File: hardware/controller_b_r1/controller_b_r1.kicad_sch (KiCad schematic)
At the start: 53 parts, among them J101 Front Pannel Connector, J102 SWD Header, J103 USB Micro B, Q101 NMOS, SW101 Reset Button, SW102 User Button, U101 NCP115ASN330T2G, U102 74LVC2T45HK3, U103 RP2040, U104 W25Q16JVUXIQ, Y101 12MHz

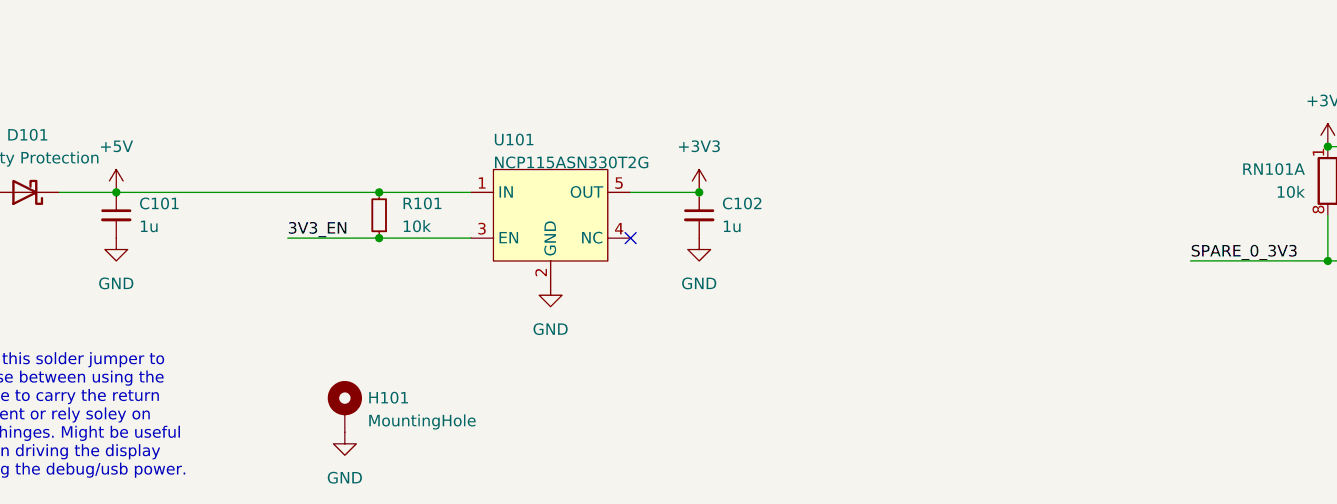
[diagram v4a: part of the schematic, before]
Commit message: First pass at the rev 2 power board.
Only did copper layers on the power board so far. Waiting to decide on a PCB fab house then I'll go back and make sure it's compliant (looking mostly at how close I can pack vias). Starting on the nucleo programmer shield next. Added a voltage divider to the enable pin on the 3V3 vreg on the controller board so it only switches on when there is enough input voltage for correct 3V3 output. I did this because I read somewhere that the RP2040 can power on at a lower voltage than a lot of flash chips and if that happens it gets into a weird state so I'm trying to make sure 3V3 comes on as quickly and sharply as possible.
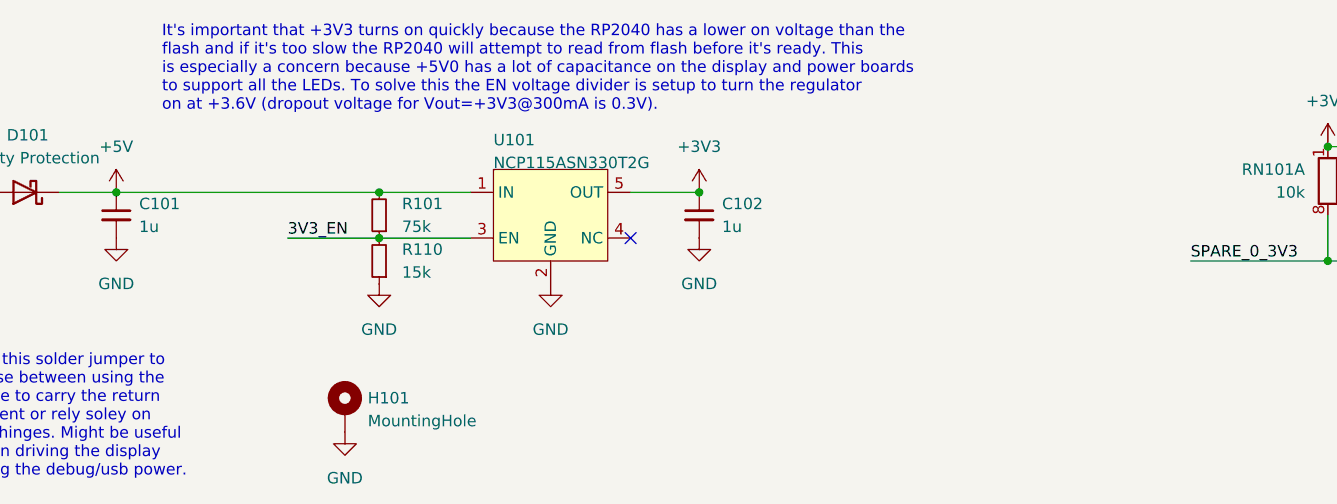
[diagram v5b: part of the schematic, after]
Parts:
- added R110: 15k, Resistor_SMD:R_0402_1005Metric, symbol Device:R_Small
- R101: value 10k -> 75k
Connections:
- net 3V3_EN: now also R110.2
- net GND: now also R110.1
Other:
- note added: "It's important that +3V3 turns on quickly because the RP2040 has a lower on voltage than the flash and if it's too slow the RP2040 will attempt to read from flash before it's ready. This is especially a concern because +5V0 has a lot of capacitance on the display and power boards to support all the LEDs. To solve this the EN voltage divider is setup to turn the regulator on at +3.6V (dropout volt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"
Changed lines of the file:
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@@
     (stroke (width 0) (type default) (color 0 0 0 0))
+  )
+  (text "It's important that +3V3 turns on quickly because the RP2040 has a lower on voltage than the\nflash and if it's too slow the RP2040 will attempt to read from flash before it's ready. This\nis especially a concern because +5V0 has a lot of capacitance on the display and power boards\nto support all the LEDs. To solve this the EN voltage divider is setup to turn the regulator\non at +3.6V (dropout voltage for Vout=+3V3@300mA is 0.3V).\n"
+    (at 77.47 25.4 0)
+    (effects (font (size 1.27 1.27)) (justify left bottom))
   )
   (text "PWM_3_A" (at 283.21 172.72 0)
@@
       (effects (font (size 1.27 1.27)) (justify right))
     )
-    (property "Value" "10k" (id 1) (at 104.14 38.0999 0)
+    (property "Value" "75k" (id 1) (at 104.14 38.0999 0)
       (effects (font (size 1.27 1.27)) (justify right))
     )
@@
     (pin "1")
   )
+  (symbol (lib_id "power:GND") (at 101.6 44.45 0) (unit 1)
+    (in_bom yes) (on_board yes) (fields_autoplaced)
+    (property "Reference" "#PWR0151" (id 0) (at 101.6 50.8 0)
+      (effects (font (size 1.27 1.27)) hide)
+    )
+    (property "Value" "GND" (id 1) (at 101.6 49.53 0))
+    (property "Footprint" "" (id 2) (at 101.6 44.45 0)
+      (effects (font (size 1.27 1.27)) hide)
+    )
+    (property "Datasheet" "" (id 3) (at 101.6 44.45 0)
+      (effects (font (size 1.27 1.27)) hide)
+    )
+    (pin "1")
+  )
   (symbol (lib_id "power:GND") (at 137.16 39.37 0) (unit 1)
     (in_bom yes) (on_board yes) (fields_autoplaced)
@@
     (pin "5")
   )
+  (symbol (lib_id "Device:R_Small") (at 101.6 41.91 180) (unit 1)
+    (in_bom yes) (on_board yes) (fields_autoplaced)
+    (property "Reference" "R110" (id 0) (at 104.14 40.6399 0)
+      (effects (font (size 1.27 1.27)) (justify right))
+    )
+    (property "Value" "15k" (id 1) (at 104.14 43.1799 0)
+      (effects (font (size 1.27 1.27)) (justify right))
+    )
+    (property "Footprint" "Resistor_SMD:R_0402_1005Metric" (id 2) (at 101.6 41.91 0)
+      (effects (font (size 1.27 1.27)) hide)
+    )
+    (property "Datasheet" "~" (id 3) (at 101.6 41.91 0)
+      (effects (font (size 1.27 1.27)) hide)
+    )
+    (pin "1")
+    (pin "2")
+  )
   (symbol (lib_id "Jumper:SolderJumper_2_Open") (at 330.2 217.17 90) (unit 1)
     (in_bom yes) (on_board yes)
@@
       (reference "#PWR0150") (unit 1) (value "VDD") (footprint "")
     )
+    (path "/9e79f1f1-5f45-41a0-96ff-06d6b5bd2da7"
+      (reference "#PWR0151") (unit 1) (value "GND") (footprint "")
+    )
     (path "/db515d74-3d0b-477b-8e05-e548a429c513"
       (reference "C101") (unit 1) (value "1u") (footprint "Capacitor_SMD:C_0402_1005Metric")
@@
     )
     (path "/82bcf8a8-0208-404b-8bd2-25710fbe3f5d"
-      (reference "R101") (unit 1) (value "10k") (footprint "Resistor_SMD:R_0402_1005Metric")
+      (reference "R101") (unit 1) (value "75k") (footprint "Resistor_SMD:R_0402_1005Metric")
     )
     (path "/901630b6-acce-49bc-9a7c-e09bfc7be616"
@@
       (reference "R109") (unit 1) (value "1k") (footprint "Resistor_SMD:R_0402_1005Metric")
     )
+    (path "/b9607c09-e293-4332-83e9-c1e94077ce90"
+      (reference "R110") (unit 1) (value "15k") (footprint "Resistor_SMD:R_0402_1005Metric")
+    )
     (path "/b68868d2-8513-482d-974f-9ce023751b7f"

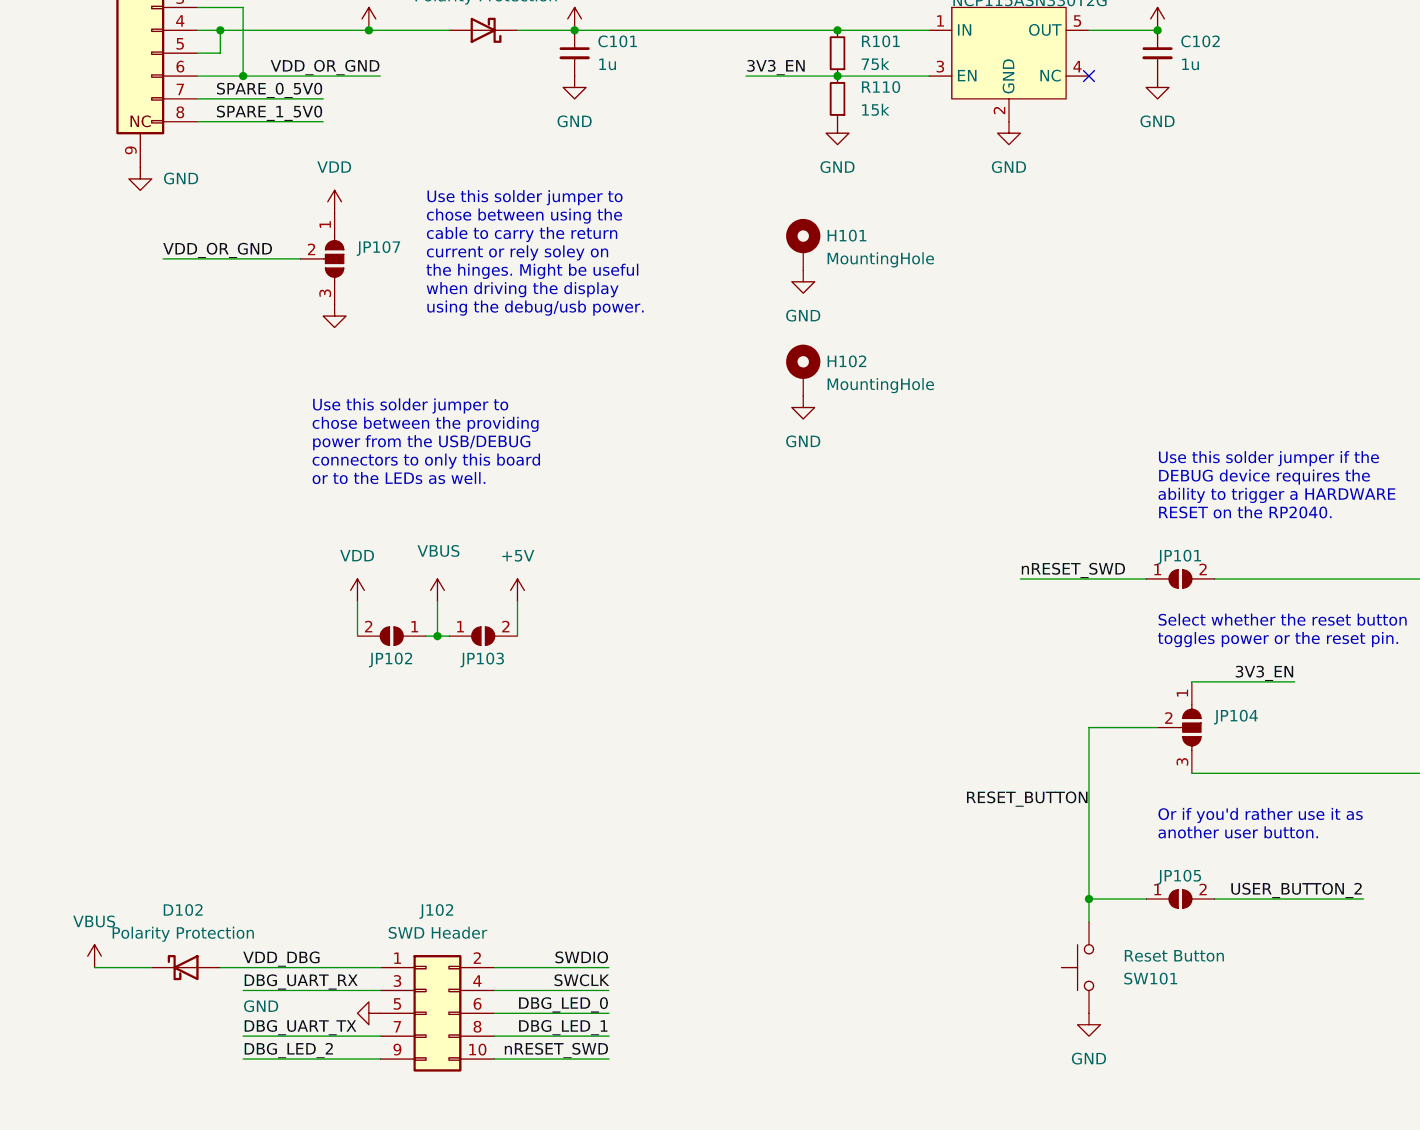
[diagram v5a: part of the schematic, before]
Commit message: Next revision of the boards are finished and ready for fabrication, and a BOM has been added.
The BOM is still missing components for the nucleo shield.
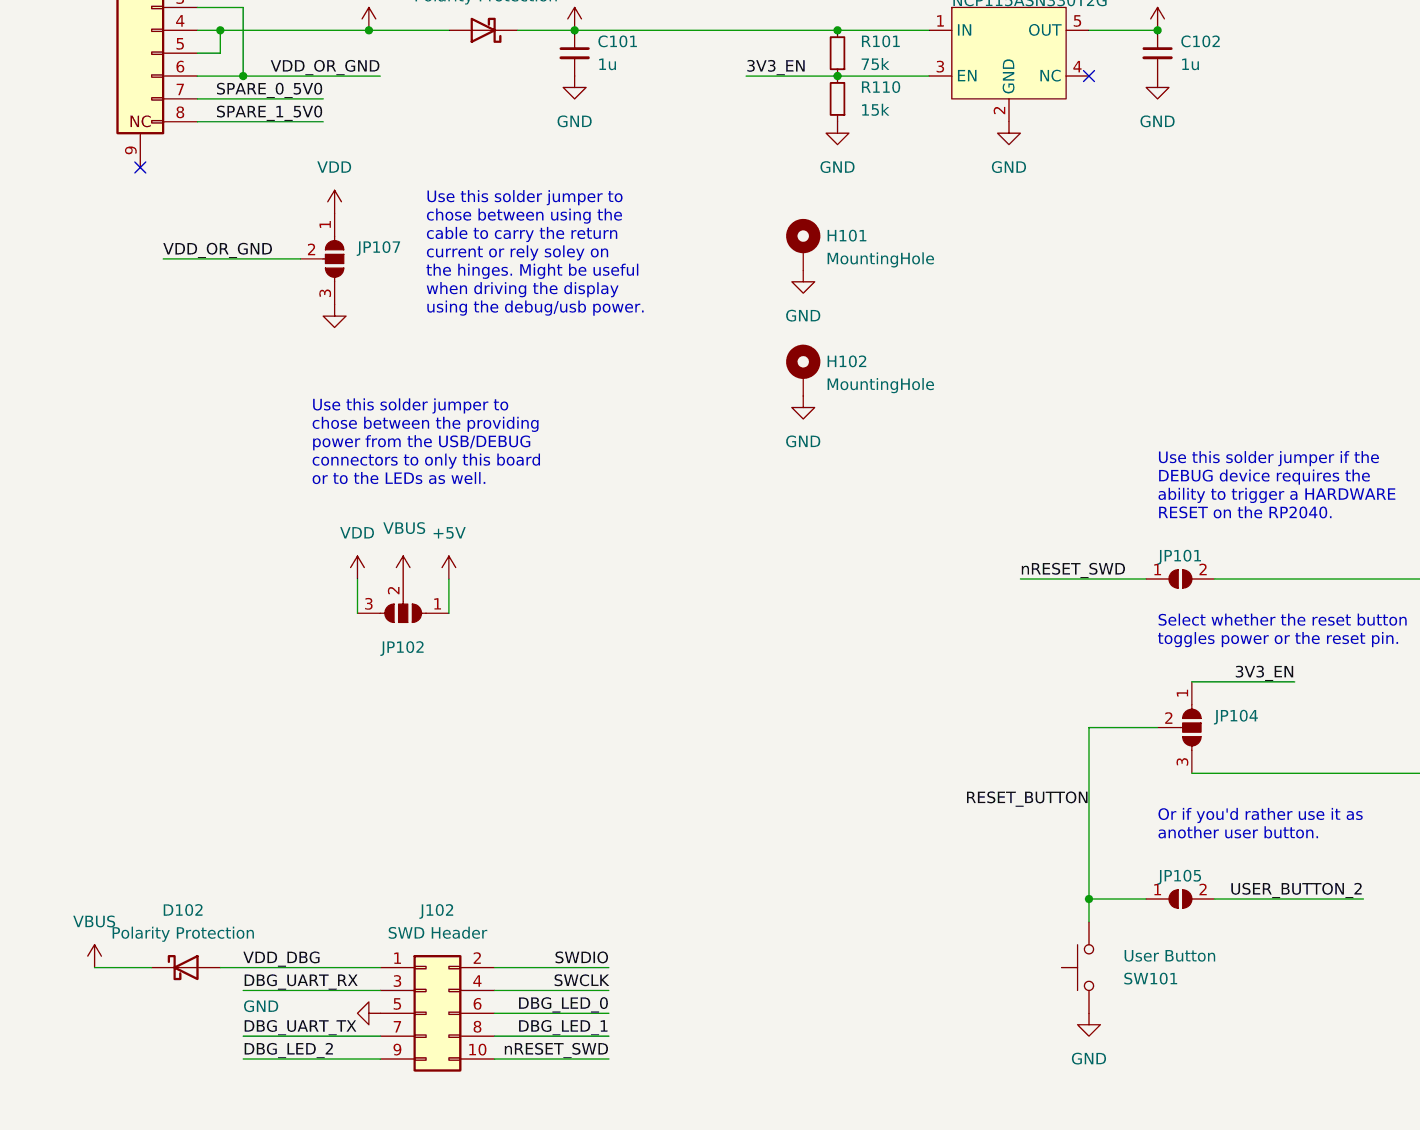
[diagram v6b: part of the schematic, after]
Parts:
- removed JP102, JP103: SolderJumper_2_Open, Jumper:SolderJumper-2_P1.3mm_Open_TrianglePad1.0x1.5mm, symbol Jumper:SolderJumper_2_Open
- added JP102: SolderJumper_3_Open, rave_shades:SolderJumper-3_P1.3mm_Open_Pad1.0x1.5mm, symbol Jumper:SolderJumper_3_Open
- C101, C102, C103, C104, C105, C106, C107, C108, C109, C110, C111, C112, C113, C114, C115, C116, C117: Item Link (none) -> https://www.digikey.com.au/en/products/detail/murata-electr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
- H101, H102, JP101, JP105, JP106: now left out of the parts list
- JP104: footprint Jumper:SolderJumper-3_P1.3mm_Open_RoundedPad1.0x1.5mm -> rave_shades:SolderJumper-3_P1.3mm_Open_Pad1.0x1.5mm; now left out of the parts list
- JP107: footprint Jumper:SolderJumper-3_P1.3mm_Open_Pad1.0x1.5mm -> rave_shades:SolderJumper-3_P1.3mm_Open_Pad1.0x1.5mm; now left out of the parts list
- R101, R102, R106, R107: Item Link (none) -> https://www.digikey.com.au/en/products/detail/bourns-inc/CR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
- R104, R105, R110: Item Link (none) -> https://www.digikey.com.au/en/products/detail/yageo/RC0402F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
- R108, R109: Item Link (none) -> https://www.digikey.com.au/en/products/detail/yageo/AC0402F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
- SW101: value Reset Button -> User Button
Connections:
- net +5V: now also JP102.1 (A)
- net GND: no longer J101.9 (NC)
- net VBUS: now also JP102.2 (C)
- net VDD: now also JP102.3 (B)
- no-connect marks 21 -> 22

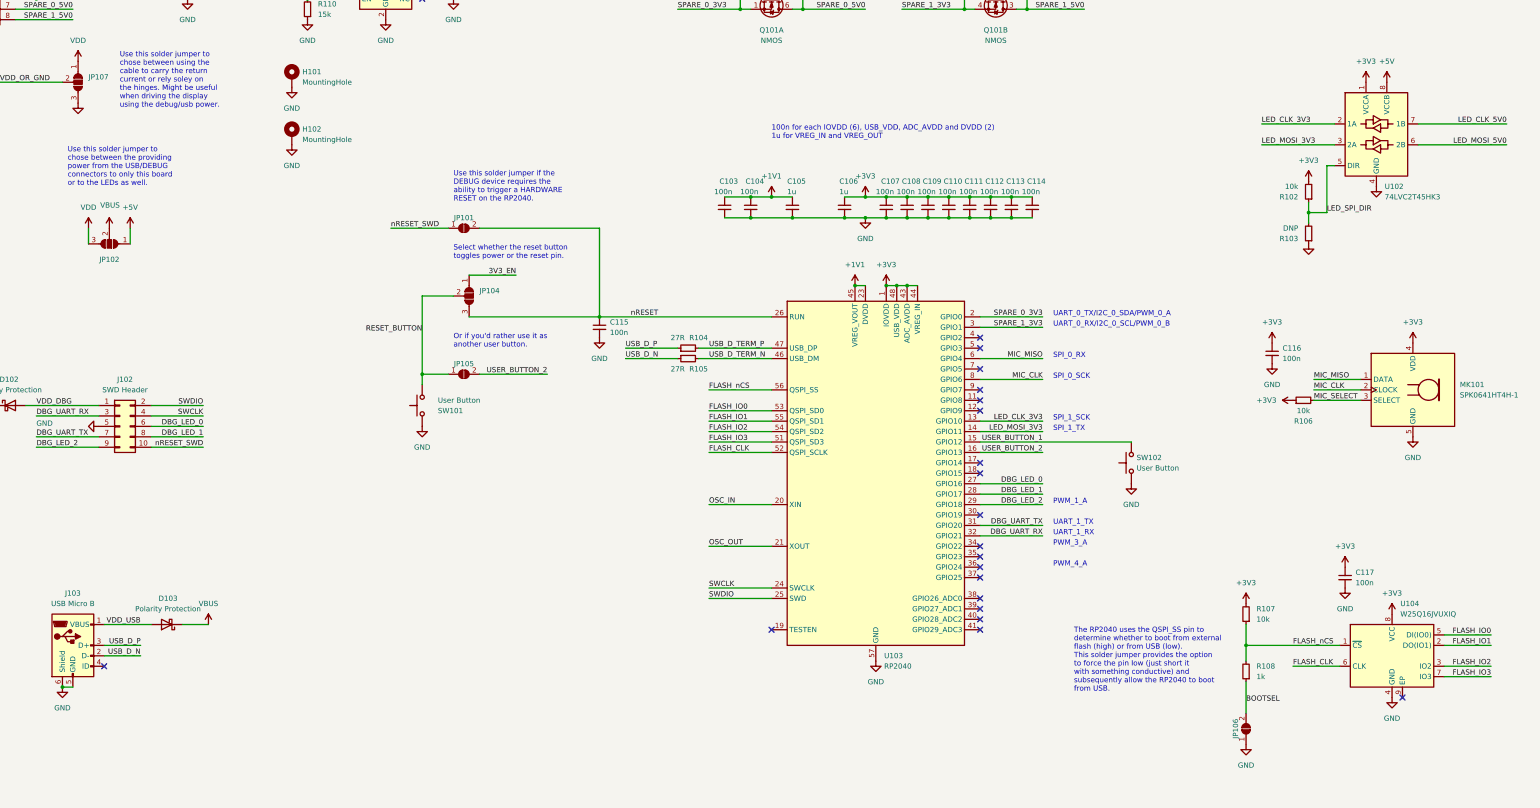
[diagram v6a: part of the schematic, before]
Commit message: Updated kicad files to work with latest kicad. Added some todos for next hw design.
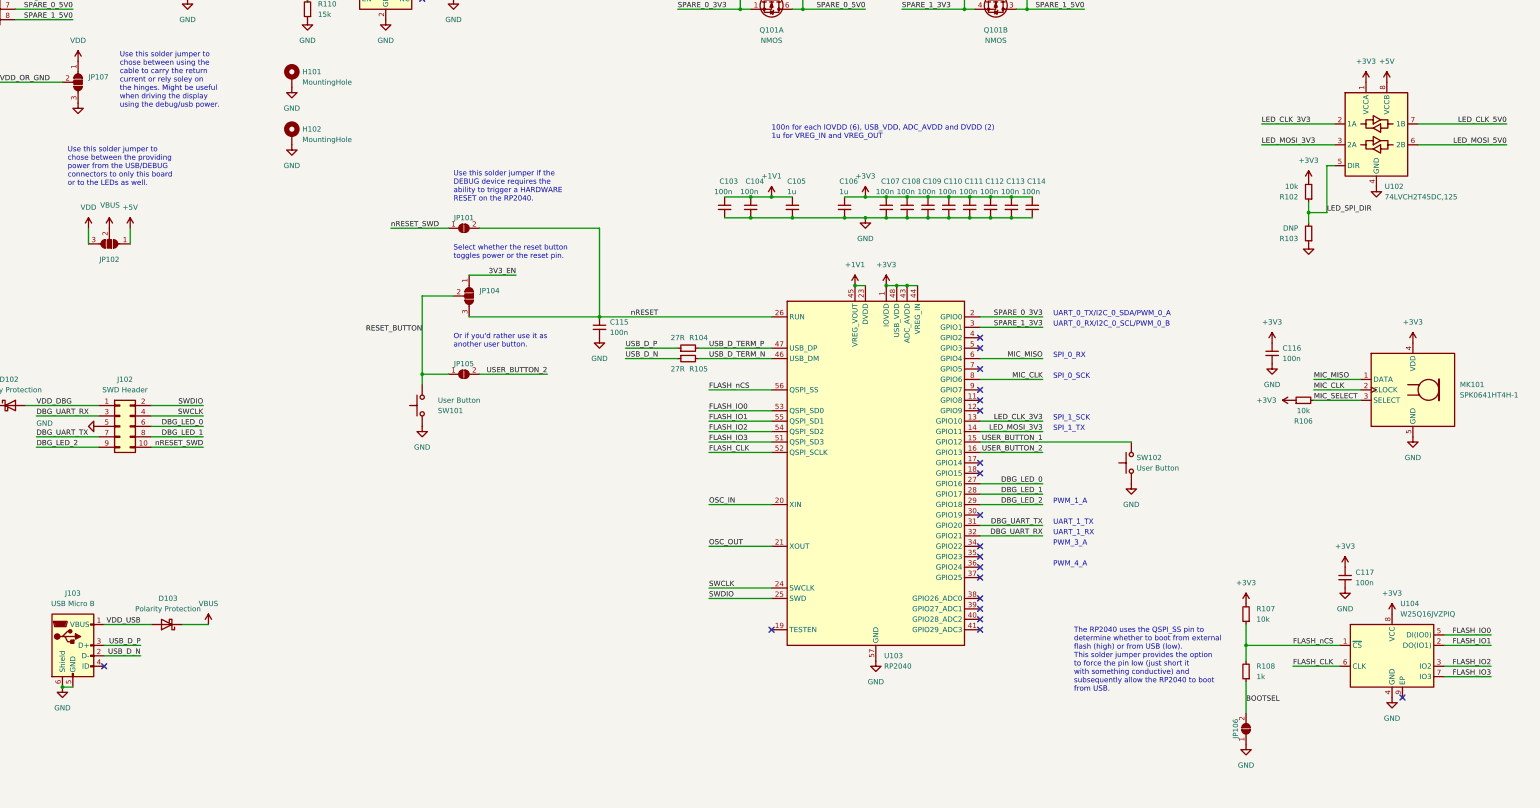
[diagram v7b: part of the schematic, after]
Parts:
- RN101: Item Link https://www.digikey.com.au/en/products/detail/panasonic-electronic-components/EXB-28V104JX/256311 -> https://www.digikey.com.au/en/products/detail/panasonic-electronic-components/EXB-28V103JX/256299
- U102: value 74LVC2T45HK3 -> 74LVCH2T45DC,125; Item Link https://www.digikey.com.au/en/products/detail/diodes-incorp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 -> https://www.digikey.com.au/en/products/detail/nexperia-usa-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
- U104: value W25Q16JVUXIQ -> W25Q16JVZPIQ; Item Link https://www.digikey.com.au/en/products/detail/winbond-electronics/W25Q16JVUXIQ-TR/15182017 -> https://www.digikey.com.au/en/products/detail/winbond-electronics/W25Q16JVZPIQ/6193770
